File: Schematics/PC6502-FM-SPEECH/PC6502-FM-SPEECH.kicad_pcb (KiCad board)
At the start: 4 copper layers, 100 x 100 mm, 76 parts, among them J1 BUS, J2 SJ-3523-SMT-TR, J5 Conn_02x05_Odd_Even, U1 ATF1502AS, U2 MCP6002-xSN, U3 MCP6002-xSN, U4 YMF262-M, U5 SP0256-AL2, U6 MCP6002-xSN, U7 YAC512-M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

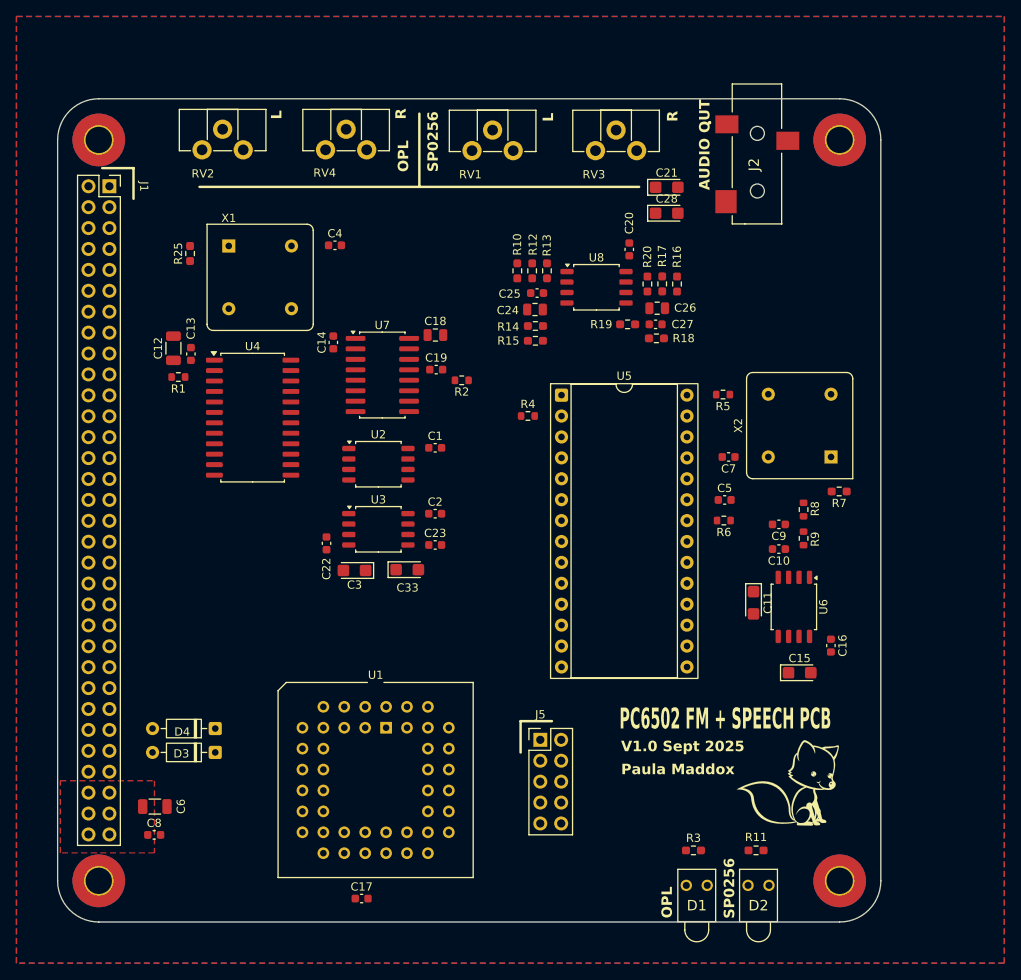
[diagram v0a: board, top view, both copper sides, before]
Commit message: Ordered Storage, FM/Speech, Dual SPI and APPLE II slot PCBs
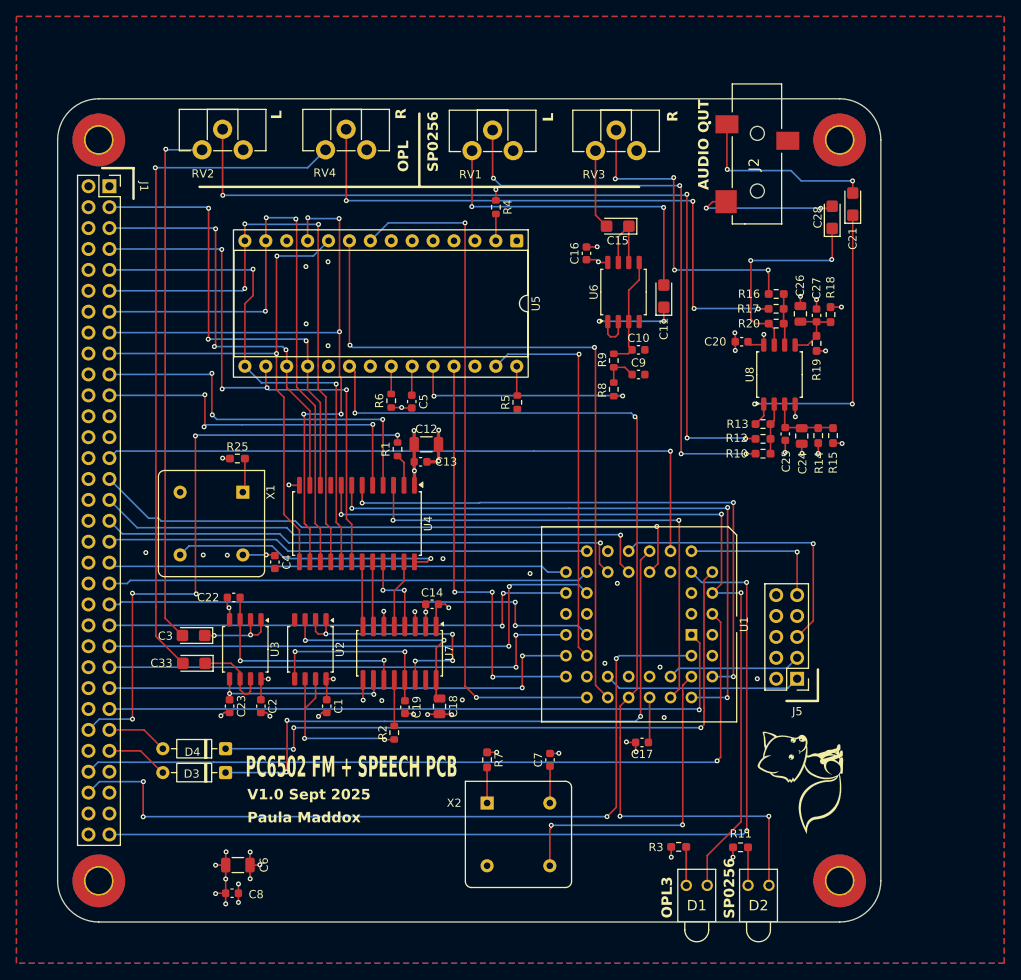
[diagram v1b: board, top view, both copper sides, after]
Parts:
- moved X2 59.3 mm to (149.2, 130.6), turned to -90 degrees
- moved C15 58.6 mm to (165.1, 60.5), turned to 180 degrees
- moved C16 56.1 mm to (161.3, 63.8), turned to 90 degrees
- moved R7 53.8 mm to (149.2, 125.3), turned to -90 degrees
- moved C18 45.1 mm to (143.4, 118.8), turned to -90 degrees
- moved R2 43.6 mm to (137.9, 122.0), turned to 90 degrees
- moved U6 43.5 mm to (165.8, 68.5), turned to 90 degrees
- moved R6 42.9 mm to (137.6, 81.7), turned to 90 degrees
- moved C7 42.7 mm to (156.9, 125.3), turned to 90 degrees
- moved C19 41.2 mm to (139.2, 118.9), turned to -90 degrees
- moved C5 39.8 mm to (140.1, 81.8), turned to -90 degrees
- moved C4 39.2 mm to (123.5, 101.3), turned to -90 degrees
- moved C17 39.0 mm to (168.1, 123.2), turned to 180 degrees
- moved C11 38.8 mm to (170.7, 69.0), turned to 90 degrees
- moved U1 38.8 mm to (174.1, 110.1), turned to -90 degrees
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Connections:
- D2 pad 1: SP0256_nALD -> SP_nALD
- U1 pad 1: unconnected-(U1-I/GCLR-Pad1) -> RnW
- U1 pad 34: /D1 -> unconnected-(U1-I/O-Pad34)
- U1 pad 36: /D0 -> unconnected-(U1-I/O-Pad36)
- U1 pad 4: RnW -> OPL3_nCS
- U1 pad 41: OPL3_nCS -> SP_OSC
- U1 pad 5: /A0 -> unconnected-(U1-I/O-Pad5)
- U5 pad 27: /SpeechSynth/SP_CLK -> SP_CLK
- X2 pad 5: /SpeechSynth/SP_CLK -> SP_OSC
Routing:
- net SP_nALD: track 0.00 -> 116.1 mm, vias 0 -> 4
- net nRES: track 0.00 -> 115.0 mm, vias 0 -> 2
- net Net-(R12-Pad1): track 0.00 -> 102.4 mm, vias 0 -> 4
- net OPL3_nCS: track 0.00 -> 100.6 mm, vias 0 -> 3
- net CPU_CLK: track 0.00 -> 96.8 mm, vias 0 -> 4
- net SYSCLK: track 0.00 -> 95.4 mm, vias 0 -> 1
- net SP_nREADY: track 0.00 -> 85.7 mm, vias 0 -> 2
- net SP_nBUSY: track 0.00 -> 84.0 mm, vias 0 -> 2
- net /OPL/OPL_OUT_B: track 0.00 -> 83.2 mm, vias 0 -> 1
- net /D6: track 0.00 -> 81.3 mm, vias 0 -> 5
- net RnW: track 0.00 -> 81.3 mm, vias 0 -> 1
- net /A4: track 0.00 -> 80.7 mm, vias 0 -> 1
- net Net-(D4-K): track 0.00 -> 79.9 mm, vias 0 -> 3
- net Net-(D3-K): track 0.00 -> 77.5 mm, vias 0 -> 3
- net /D5: track 0.00 -> 76.9 mm, vias 0 -> 3
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- removed copper zone on F.Cu, net +5V
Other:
- board text added: "OPL3"

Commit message: CPU CPLD UPDATE!!
CPU will now run at 14MHz with the updated code in the CPLD
Begun assembly of Speech/FM board
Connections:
- U1 pad 34: unconnected-(U1-I/O-Pad34) -> /D1
- U1 pad 36: unconnected-(U1-I/O-Pad36) -> /D0
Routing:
- net /D0: track 58.3 -> 126.0 mm, vias 3 -> 5
- net /D1: track 53.8 -> 120.3 mm, vias 3 -> 5
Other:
- board text added: "V1.1 Oct 2025"
- board text removed: "V1.0 Sept 2025"
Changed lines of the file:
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@@
 	(net 111 "Net-(J2-SLEEVE)")
 	(net 112 "Net-(J2-TIP)")
-	(net 113 "unconnected-(U1-I{slash}O-Pad36)")
-	(net 114 "unconnected-(U1-I{slash}O-Pad5)")
-	(net 115 "unconnected-(U1-I{slash}O-Pad34)")
+	(net 113 "unconnected-(U1-I{slash}O-Pad5)")
 	(footprint "MountingHole:MountingHole_3.2mm_M3_Pad_TopBottom"
 		(layer "F.Cu")
@@
 			(layers "*.Cu" "*.Mask")
 			(remove_unused_layers no)
-			(net 114 "unconnected-(U1-I{slash}O-Pad5)")
+			(net 113 "unconnected-(U1-I{slash}O-Pad5)")
 			(pinfunction "I/O")
 			(pintype "bidirectional+no_connect")
@@
 			(layers "*.Cu" "*.Mask")
 			(remove_unused_layers no)
-			(net 115 "unconnected-(U1-I{slash}O-Pad34)")
+			(net 3 "/D1")
 			(pinfunction "I/O")
-			(pintype "bidirectional+no_connect")
+			(pintype "bidirectional")
 		)
 		(pad "35" thru_hole circle
@@
 			(layers "*.Cu" "*.Mask")
 			(remove_unused_layers no)
-			(net 113 "unconnected-(U1-I{slash}O-Pad36)")
+			(net 2 "/D0")
 			(pinfunction "I/O")
-			(pintype "bidirectional+no_connect")
+			(pintype "bidirectional")
 		)
 		(pad "37" thru_hole circle
@@
 		)
 	)
-	(gr_text "V1.0 Sept 2025"
+	(gr_text "V1.1 Oct 2025"
 		(at 120.09 130.256 0)
 		(layer "F.SilkS")
@@
 	)
 	(segment
+		(start 170.4848 89.8652)
+		(end 170.4848 102.922267)
+		(width 0.2)
+		(layer "F.Cu")
+		(net 2)
+	)
+	(segment
 		(start 127.43 74.58)
 		(end 127.43 77.49)
@@
 	)
 	(segment
+		(start 170.18 89.5604)
+		(end 170.4848 89.8652)
+		(width 0.2)
+		(layer "F.Cu")
+		(net 2)
+	)
+	(segment
+		(start 168.97 104.437067)
+		(end 168.97 115.19)
+		(width 0.2)
+		(layer "F.Cu")
+		(net 2)
+	)
+	(segment
+		(start 128.975 91.95)
+		(end 128.975 89.8652)
+		(width 0.2)
+		(layer "F.Cu")
+		(net 2)
+	)
+	(segment
 		(start 127.25 74.4)
 		(end 127.43 74.58)
@@
 	)
 	(segment
-		(start 128.975 91.95)
+		(start 170.4848 102.922267)
+		(end 168.97 104.437067)
+		(width 0.2)
+		(layer "F.Cu")
+		(net 2)
+	)
+	(segment
+		(start 128.975 89.8652)
 		(end 128.975 81.9)
 		(width 0.2)
@@
 	)
 	(via
+		(at 170.18 89.5604)
+		(size 0.6)
+		(drill 0.3)
+		(layers "F.Cu" "B.Cu")
+		(net 2)
+	)
+	(via
+		(at 128.975 89.8652)
+		(size 0.6)
+		(drill 0.3)
+		(layers "F.Cu" "B.Cu")
+		(net 2)
+	)
+	(via
 		(at 115.35 74.2)
 		(size 0.6)
@@
 	)
 	(segment
+		(start 143.639543 89.5604)
+		(end 143.598943 89.601)
+		(width 0.2)
+		(layer "B.Cu")
+		(net 2)
+	)
+	(segment
 		(start 115.35 74.2)
 		(end 127.05 74.2)
@@
 	)
 	(segment
+		(start 143.101057 89.601)
+		(end 143.060457 89.5604)
+		(width 0.2)
+		(layer "B.Cu")
+		(net 2)
+	)
+	(segment
 		(start 127.05 74.2)
 		(end 127.25 74.4)
@@
 	)
 	(segment
+		(start 143.060457 89.5604)
+		(end 129.2798 89.5604)
+		(width 0.2)
+		(layer "B.Cu")
+		(net 2)
+	)
+	(segment
+		(start 129.2798 89.5604)
+		(end 128.975 89.8652)
+		(width 0.2)
+		(layer "B.Cu")
+		(net 2)
+	)
+	(segment
+		(start 170.18 89.5604)
+		(end 143.639543 89.5604)
+		(width 0.2)
+		(layer "B.Cu")
+		(net 2)
+	)
+	(segment
 		(start 103.35 58.165)
 		(end 115.265 58.165)
@@
 	)
 	(segment
+		(start 143.598943 89.601)
+		(end 143.101057 89.601)
+		(width 0.2)
+		(layer "B.Cu")
+		(net 2)
+	)
+	(segment
 		(start 124.89 77.49)
 		(end 124.89 80.09)
@@
 	)
 	(segment
+		(start 164.9022 86.6702)
+		(end 164.6936 86.4616)
+		(width 0.2)
+		(layer "F.Cu")
+		(net 3)
+	)
+	(segment
 		(start 124.89 75.59)
 		(end 124.8 75.5)
@@
 	)
 	(segment
+		(start 166.43 103.921467)
+		(end 164.9022 102.393667)
+		(width 0.2)
+		(layer "F.Cu")
+		(net 3)
+	)
+	(segment
 		(start 124.89 80.09)
 		(end 127.705 82.905)
@@
 	)
 	(segment
+		(start 164.9022 102.393667)
+		(end 164.9022 86.6702)
+		(width 0.2)
+		(layer "F.Cu")
+		(net 3)
+	)
+	(segment
 		(start 127.705 82.905)
-		(end 127.705 91.95)
+		(end 127.705 86.614)
 		(width 0.2)
 		(layer "F.Cu")
@@
 		(net 3)
 	)
+	(segment
+		(start 127.705 86.614)
+		(end 127.705 91.95)
+		(width 0.2)
+		(layer "F.Cu")
+		(net 3)
+	)
+	(segment
+		(start 166.43 115.19)
+		(end 166.43 103.921467)
+		(width 0.2)
+		(layer "F.Cu")
+		(net 3)
+	)
 	(via
 		(at 124.8 75.5)
@@
 	)
 	(via
+		(at 127.705 86.614)
+		(size 0.6)
+		(drill 0.3)
+		(layers "F.Cu" "B.Cu")
+		(net 3)
+	)
+	(via
 		(at 116.1 75.1)
 		(size 0.6)
@@
 		(net 3)
 	)
+	(via
+		(at 164.6936 86.4616)
+		(size 0.6)
+		(drill 0.3)
+		(layers "F.Cu" "B.Cu")
+		(net 3)
+	)
+	(segment
+		(start 164.6936 86.4616)
+		(end 127.8574 86.4616)
+		(width 0.2)
+		(layer "B.Cu")
+		(net 3)
+	)
 	(segment
 		(start 124.4 75.1)
@@
 	)
 	(segment
+		(start 127.8574 86.4616)
+		(end 127.705 86.614)
+		(width 0.2)
+		(layer "B.Cu")
+		(net 3)
+	)
+	(segment
 		(start 103.35 60.705)
 		(end 116.155 60.705)
@@
 	)
 	(segment
-		(start 165.45 98)
+		(start 165.5076 97.9424)
 		(end 165.4178 98.0322)
 		(width 0.2)
@@
 		(net 16)
 	)
+	(segment
+		(start 165.608 97.9424)
+		(end 165.5076 97.9424)
+		(width 0.2)
+		(layer "F.Cu")
+		(net 16)
+	)
 	(via
-		(at 165.45 98)
+		(at 165.608 97.9424)
 		(size 0.6)
 		(drill 0.3)
@@
 	)
 	(segment
-		(start 124.9 97.1)
-		(end 125.75 97.95)
+		(start 106.725 97.1)
+		(end 103.35 93.725)
 		(width 0.2)
 		(layer "B.Cu")
@@
 	)
 	(segment
-		(start 103.35 93.725)
+		(start 124.9 97.1)
 		(end 106.725 97.1)
 		(width 0.2)
@@
 	)
 	(segment
-		(start 125.75 97.95)
+		(start 165.4076 97.9424)
 		(end 165.4 97.95)
 		(width 0.2)
@@
 	)
 	(segment
-		(start 106.725 97.1)
+		(start 165.608 97.9424)
+		(end 165.4076 97.9424)
+		(width 0.2)
+		(layer "B.Cu")
+		(net 16)
+	)
+	(segment
+		(start 125.75 97.95)
 		(end 124.9 97.1)
 		(width 0.2)
@@
 	(segment
 		(start 165.4 97.95)
-		(end 165.45 98)
+		(end 125.75 97.95)
 		(width 0.2)
 		(layer "B.Cu")
@@
 	)
 	(segment
-		(start 148.351 94.049)
-		(end 179.149 94.049)
-		(width 0.2)
-		(layer "B.Cu")
-		(net 92)
-	)
-	(segment
-		(start 148.3 94.1)
-		(end 148.351 94.049)
+		(start 176.59 115.19)
+		(end 179.14 115.19)
 		(width 0.2)
 		(layer "B.Cu")
@@
 	)
 	(segment
-		(start 176.59 115.19)
-		(end 179.14 115.19)
+		(start 179.14 115.19)
+		(end 179.15 115.2)
 		(width 0.2)
 		(layer "B.Cu")
@@
 	)
 	(segment
-		(start 179.14 115.19)
-		(end 179.15 115.2)
+		(start 134.101 94.049)
+		(end 179.149 94.049)
 		(width 0.2)
 		(layer "B.Cu")
@@
 	(segment
 		(start 134.05 94.1)
-		(end 148.3 94.1)
+		(end 134.101 94.049)
 		(width 0.2)
 		(layer "B.Cu")

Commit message: SP0256 Speech synth working
SP0256 now working, couple of extra wires needed, but PCB and schematics updated.
Test code (SP0256_TEST3.BAS) created.
CPLD updated.
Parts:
- added C29: 0.1u, Capacitor_SMD:C_0603_1608Metric, F.Cu at (152.8, 58.2)
- R4: value 0R -> 100K
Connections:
- R4 pad 2: Net-(U5-~{RESET}) -> SP_nRST
- U1 pad 5: unconnected-(U1-I/O-Pad5) -> /A0
- U5 pad 2: Net-(U5-~{RESET}) -> SP_nRST
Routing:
- net /A0: track 46.5 -> 106.7 mm, vias 3 -> 4
- net SP_nRST: track 51.3 -> 76.9 mm, vias 3 -> 4
- net GND: track 44.9 -> 48.1 mm
- net Net-(U5-~{RESET}): track 3.26 -> 0.00 mm

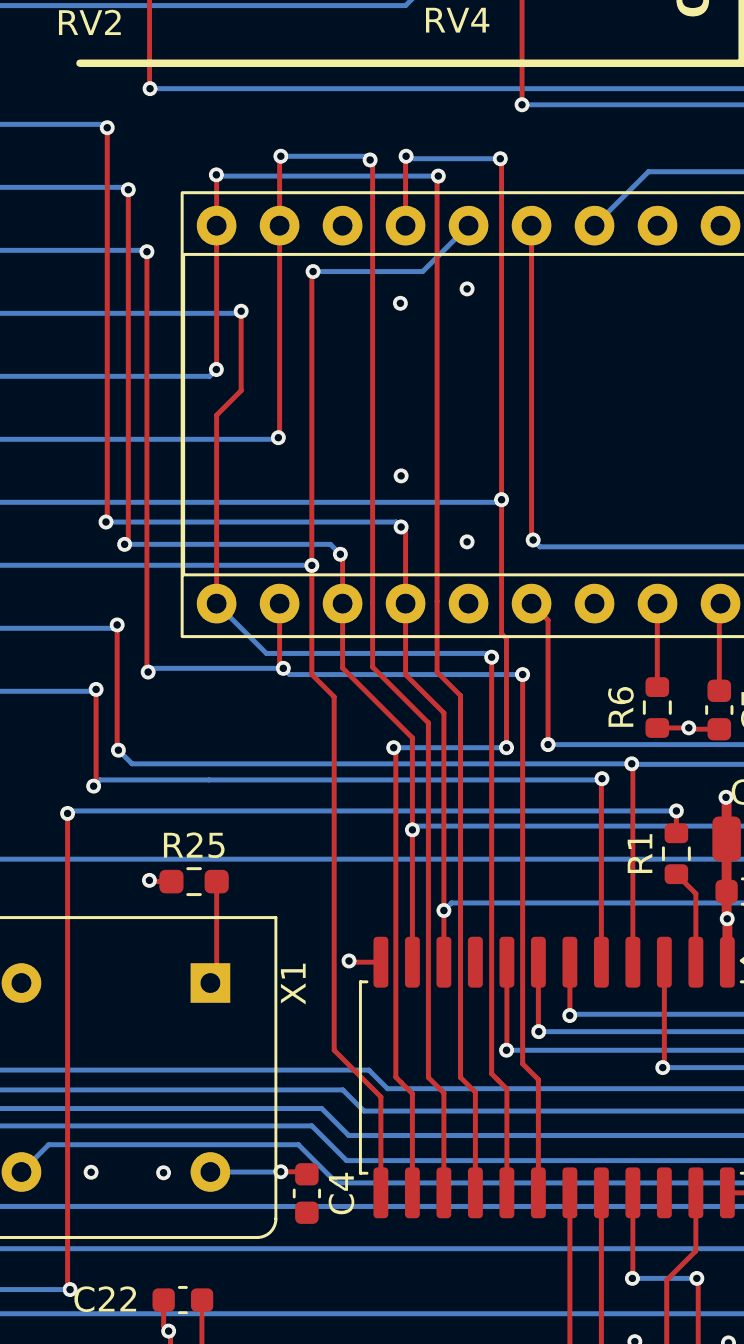
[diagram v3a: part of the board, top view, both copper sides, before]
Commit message: Updated Schematics and CPLD files
Files updated for the CPU & FM Speech board
Also revised CPLDs for CPU, VIA and Compact Flasg
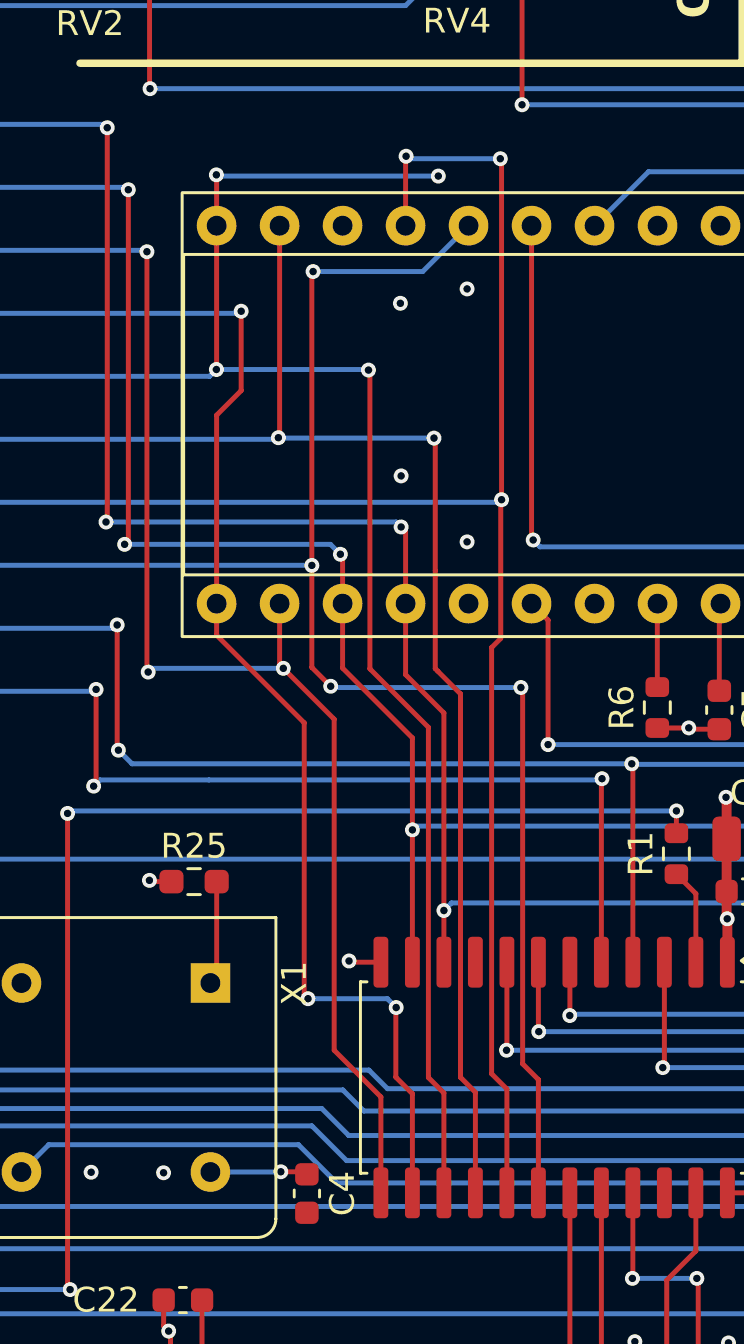
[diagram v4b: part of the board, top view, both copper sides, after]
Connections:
- U4 pad 13: /D7 -> /D2
- U4 pad 14: /D6 -> /D3
- U4 pad 15: /D5 -> /D4
- U4 pad 16: /D4 -> /D5
- U4 pad 17: /D3 -> /D6
- U4 pad 18: /D2 -> /D7
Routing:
- net /D5: track 76.9 -> 65.0 mm, vias 3 -> 2
- net /D2: track 69.7 -> 61.6 mm, vias 4 -> 3
- net /D7: track 65.7 -> 72.8 mm, vias 2 -> 4
- net /D3: track 63.5 -> 58.6 mm, vias 2 -> 3
- net /D6: track 81.3 -> 76.8 mm, vias 5 -> 3
- net /D4: track 75.1 -> 74.0 mm, vias 3 -> 4
